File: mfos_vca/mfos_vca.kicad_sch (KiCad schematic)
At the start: 14 parts, among them J1 CV1, J2 CV1, Q1 2N3904, Q2 2N3906, SW1 SW_SPDT, U1 TL074

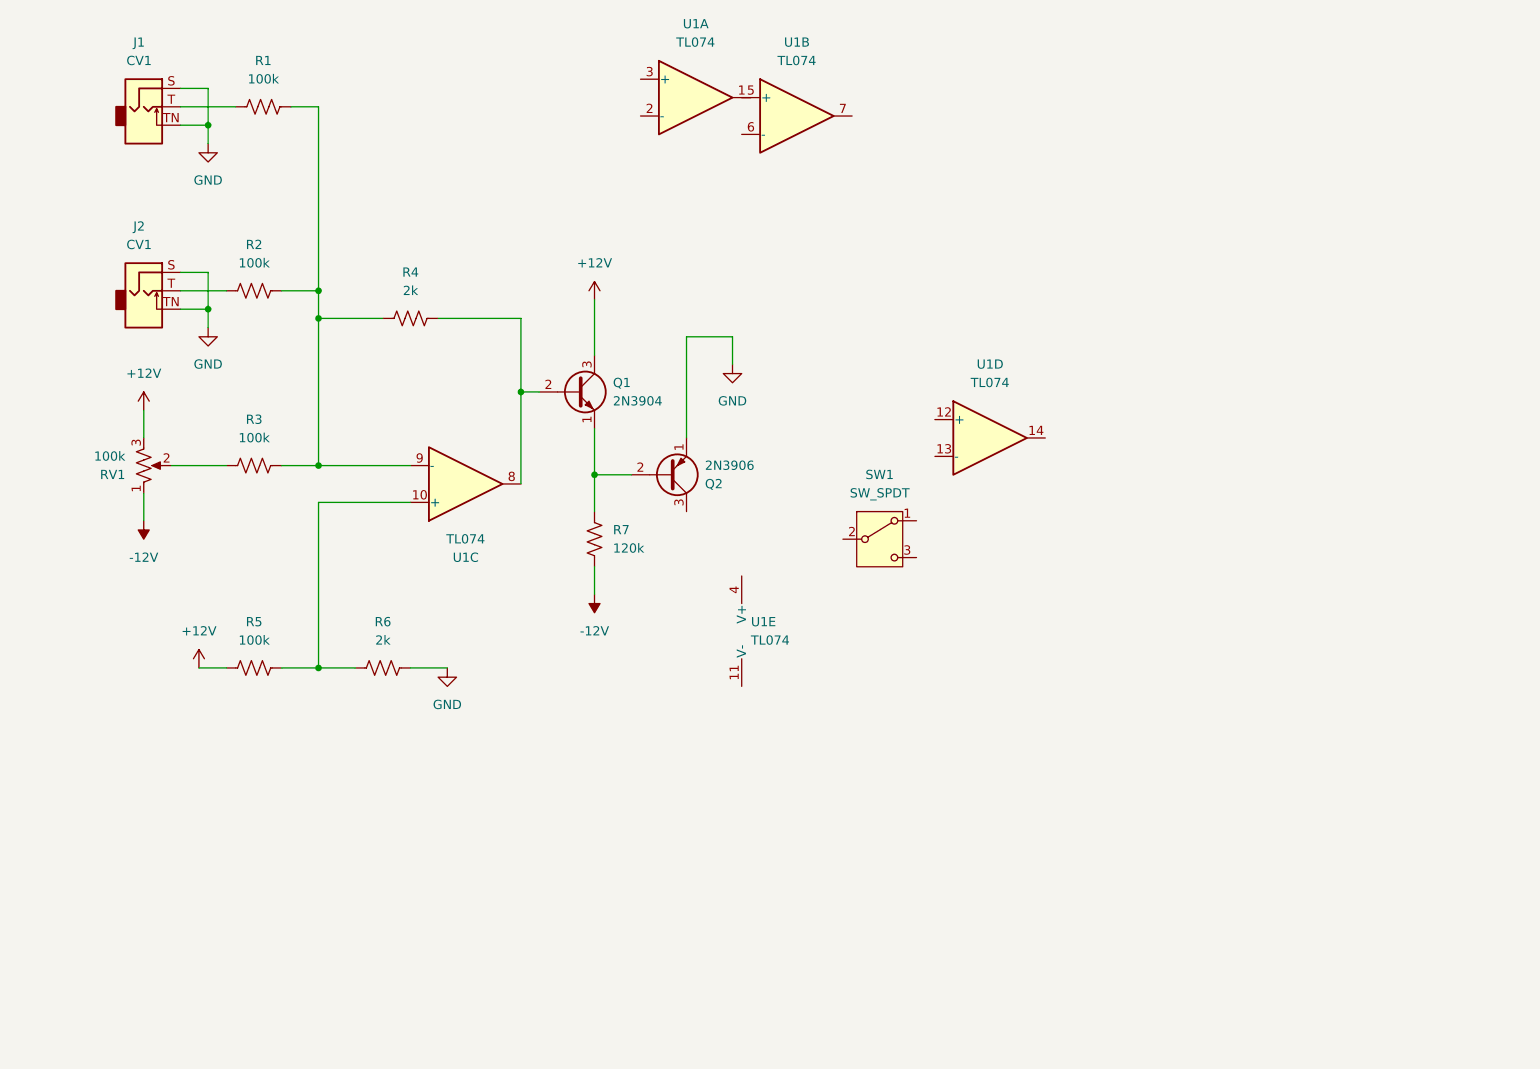
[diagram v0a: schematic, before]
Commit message: Mostly finish VCA-A schematic
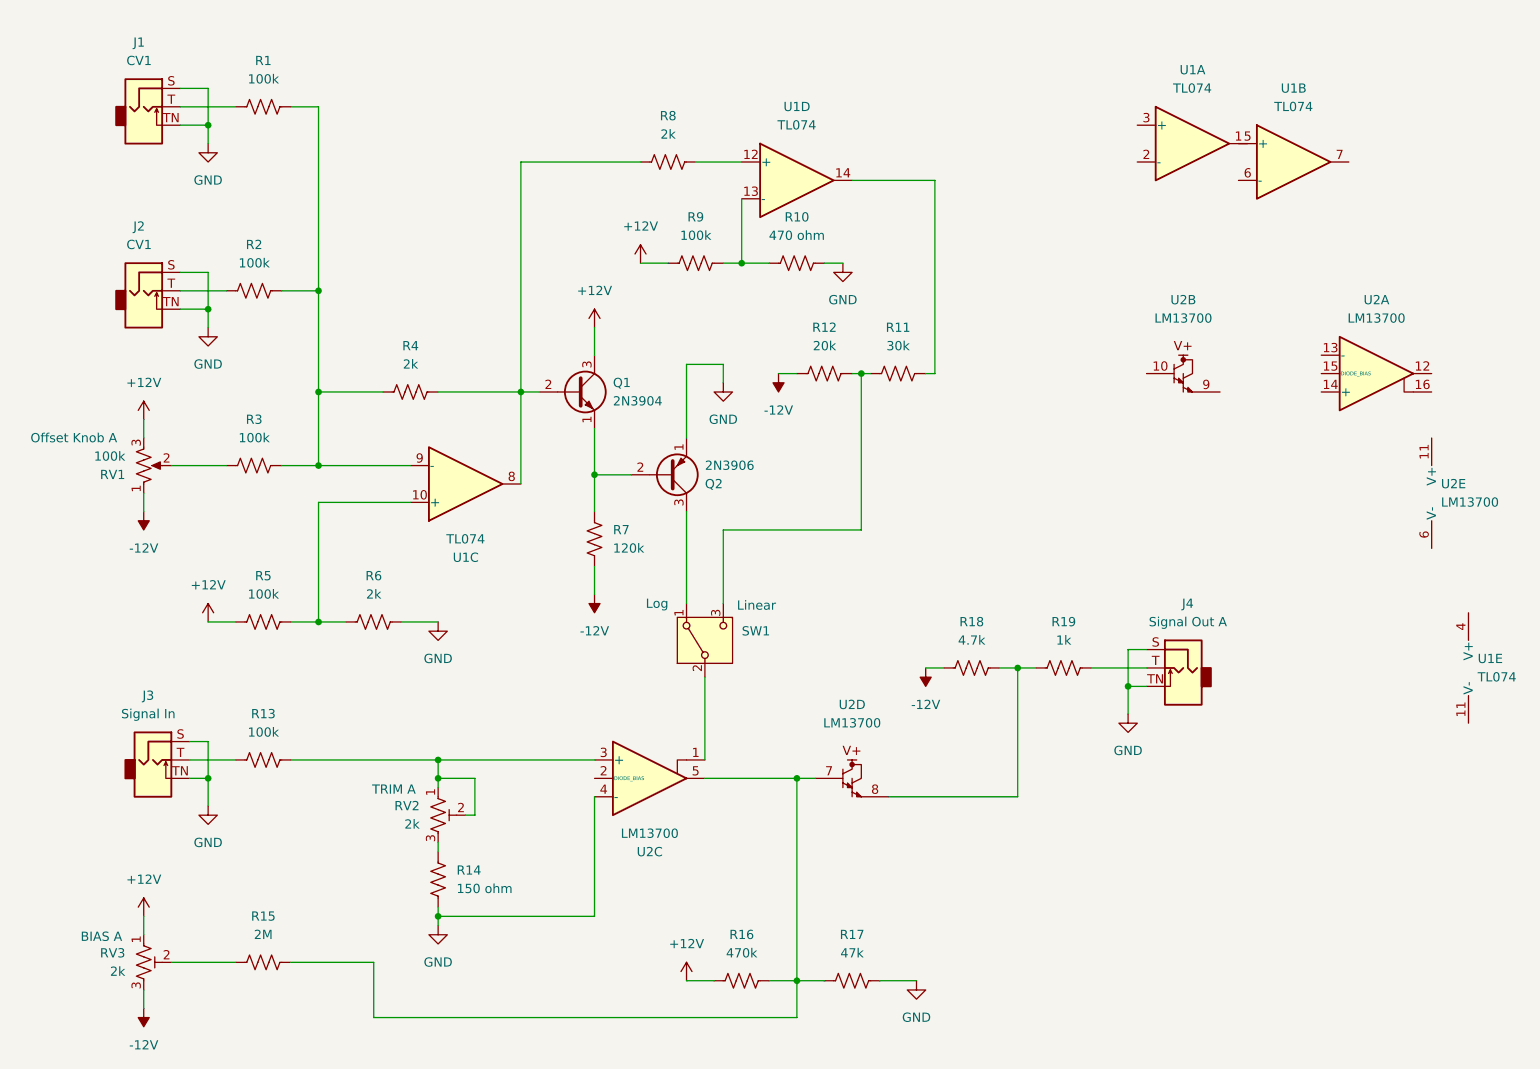
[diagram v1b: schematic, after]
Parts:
- added J3: Signal In, symbol Connector_Audio:AudioJack2_SwitchT
- added J4: Signal Out A, symbol Connector_Audio:AudioJack2_SwitchT
- added R10: 470 ohm, symbol Device:R_US
- added R11: 30k, symbol Device:R_US
- added R12: 20k, symbol Device:R_US
- added R13, R9: 100k, symbol Device:R_US
- added R14: 150 ohm, symbol Device:R_US
- added R15: 2M, symbol Device:R_US
- added R16: 470k, symbol Device:R_US
- added R17: 47k, symbol Device:R_US
- added R18: 4.7k, symbol Device:R_US
- added R19: 1k, symbol Device:R_US
- added R8: 2k, symbol Device:R_US
- added RV2, RV3: 2k, symbol Device:R_Potentiometer_Trim_US
- added U2: LM13700, symbol Amplifier_Operational:LM13700
- RV1: Label (none) -> Offset Knob A
- SW1: Label1 (none) -> Log; Label2 (none) -> Linear
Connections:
- net +12V: now also R16.1, R9.1, RV3.1
- net -12V: now also R12.1, R18.1, RV3.3
- net GND: now also J3.S, J3.TN, J4.S, J4.TN, R10.2, R14.2, R17.2, U2.4 (-)
- net at Q2.3 (C): now also SW1.1 (A)
- net at Q1.2 (B), R4.2, U1.8: now also R8.1
- net at SW1.2 (B): now also U2.1
- net at SW1.3 (C): now also R11.1, R12.2
- net at U1.12 (+): now also R8.2
- net at U1.13 (-): now also R10.1, R9.2
- net at U1.14: now also R11.2
- new net: J3.T, R13.1
- new net: R13.2, RV2.1, RV2.2, U2.3 (+)
- new net: R15.2, R16.2, R17.1, U2.5, U2.7
- new net: R18.2, R19.1, U2.8
- new net: R15.1, RV3.2
- new net: R14.1, RV2.3
- new net: J4.T, R19.2
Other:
- company: (none) -> Jesse Holzman
- title: (none) -> MFOS Dual VCA
- moved on the sheet: R4, R5, R6, SW1, U1A, U1B, U1D, U1E

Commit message: Add schematic for  second VCA
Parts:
- added D1, D2: 1N5819, symbol Device:D_Schottky
- added J5: CV1 B, symbol Connector_Audio:AudioJack2_SwitchT
- added J6: CV2 B, symbol Connector_Audio:AudioJack2_SwitchT
- added J7: Signal In B, symbol Connector_Audio:AudioJack2_SwitchT
- added J8: Signal Out A, symbol Connector_Audio:AudioJack2_SwitchT
- added J?: Conn_02x05_Odd_Even, symbol Connector_Generic:Conn_02x05_Odd_Even
- added Q3: 2N3904, Package_TO_SOT_THT:TO-92_Inline, symbol Transistor_BJT:2N3904
- added Q4: 2N3906, Package_TO_SOT_THT:TO-92_Inline, symbol Transistor_BJT:2N3906
- added R20, R21, R22, R23, R24, R31: 100k, symbol Device:R_US
- added R25: 2M, symbol Device:R_US
- added R26, R27, R30: 2k, symbol Device:R_US
- added R28: 150 ohm, symbol Device:R_US
- added R29: 120k, symbol Device:R_US
- added R32: 470k, symbol Device:R_US
- added R33: 470 ohm, symbol Device:R_US
- added R34: 20k, symbol Device:R_US
- added R35: 47k, symbol Device:R_US
- added R36: 30k, symbol Device:R_US
- added R37: 4.7k, symbol Device:R_US
- added R38: 1k, symbol Device:R_US
- added RV4: 100k, symbol Device:R_Potentiometer_US
- added RV5, RV6: 2k, symbol Device:R_Potentiometer_Trim_US
- added SW2: SW_SPDT, symbol Switch:SW_SPDT
- J1: value CV1 -> CV1 A
- J2: value CV1 -> CV2 A
- J3: value Signal In -> Signal In A
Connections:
- net +12V: now also Q3.3 (C), R23.1, R31.1, R32.1, RV4.3, RV5.1
- net -12V: now also R29.1, R34.1, R37.1, RV4.1, RV5.3
- net GND: now also U2.14 (+), J5.S, J5.TN, J6.S, J6.TN, J7.S, J7.TN, J8.S, J8.TN, J?.3 (Pin_3), J?.4 (Pin_4), J?.5 (Pin_5), J?.6 (Pin_6), J?.7 (Pin_7), J?.8 (Pin_8), Q4.1 (E), R26.2, R28.2, R33.2, R35.2
- net at U2.10: now also U2.16, R25.2, R32.2, R35.1
- net at U2.9: now also R37.2, R38.1
- net at U2.12: now also SW2.2 (B)
- net at U2.13 (-): now also R24.2, RV6.1, RV6.2
- net at U1.1: now also R36.2
- net at U1.2 (-): now also R31.2, R33.1
- net at U1.3 (+): now also R30.2
- net at U1.5 (+): now also R20.2, R21.2, R22.2, R27.1
- net at U1.6 (-): now also R23.2, R26.1
- net at U1.7: now also Q3.2 (B), R27.2, R30.1
- new net: Q4.3 (C), SW2.1 (A)
- new net: R34.2, R36.1, SW2.3 (C)
- new net: J7.T, R24.1
- new net: R21.1, RV4.2
- new net: Q3.1 (E), Q4.2 (B), R29.2
- new net: D2.1 (K), J?.1 (Pin_1), J?.2 (Pin_2)
- new net: R28.1, RV6.3
- new net: J8.T, R38.2
- new net: J6.T, R20.1
- new net: R25.1, RV5.2
- new net: D1.2 (A), J?.10 (Pin_10), J?.9 (Pin_9)
- new net: J5.T, R22.1
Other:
- moved on the sheet: R15, RV3, U1A, U1B, U1E, U2A, U2B, U2D, U2E

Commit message: Finish VCA schematic
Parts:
- added C1, C2: 47uF, symbol Device:C_Polarized_Small_US
- added C3, C4, C5, C6, C7, C8: 0.1uF, symbol Device:C_Small
- added R39, R40: 10 ohm, symbol Device:R_US
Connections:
- net +12V: now also U1.4 (V+), U2.11 (V+), C1.1, C3.1, C5.1, C7.1, R39.2
- net -12V: now also U1.11 (V-), U2.6 (V-), C2.2, C4.2, C6.2, C8.2, R40.2
- net GND: now also C1.2, C2.1, C3.2, C4.1, C5.2, C6.1, C7.2, C8.1
- net at D2.2 (A): now also R40.1
- net at D1.1 (K): now also R39.1
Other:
- moved on the sheet: D1, D2, J1, J2, J3, J4, J5, J6, J7, J8, J?, Q1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

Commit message: Assign footprints
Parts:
- C1, C2: footprint (none) -> Capacitor_THT:CP_Radial_D6.3mm_P2.50mm
- C3, C4, C5, C6, C7, C8: footprint (none) -> Capacitor_THT:C_Rect_L7.2mm_W2.5mm_P5.00mm
- D1, D2: footprint (none) -> Diode_THT:D_DO-41_SOD81_P7.62mm_Horizontal
- J1, J2, J3, J4, J5, J6, J7, J8, RV1, RV4: footprint (none) -> Connector_PinHeader_2.54mm:PinHeader_1x03_P2.54mm_Vertical
- J9: renamed from J?; footprint (none) -> Connector_IDC:IDC-Header_2x05_P2.54mm_Vertical
- R1, R10, R11, R12, R13, R14, R15, R16, R17, R18, R19, R2, R20, R21, R22, R23, R24, R25, R26, R27, R28, R29, R3, R30, R31, R32, R33, R34, R35, R36, R37, R38, R39, R4, R40, R5, R6, R7, R8, R9: footprint (none) -> Resistor_THT:R_Axial_DIN0207_L6.3mm_D2.5mm_P10.16mm_Horizontal
- RV2, RV6: footprint (none) -> Potentiometer_THT:Potentiometer_Bourns_3296W_Vertical
- RV3, RV5: value 2k -> 100k; footprint (none) -> Potentiometer_THT:Potentiometer_Piher_PT-6-V_Vertical
- U1: footprint (none) -> Package_DIP:DIP-14_W7.62mm_Socket
- U2: footprint (none) -> Package_DIP:DIP-16_W7.62mm_Socket

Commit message: Remove secondary CV input per VCA, some more panel progress
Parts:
- removed J1: CV1 A, Connector_PinHeader_2.54mm:PinHeader_1x03_P2.54mm_Vertical, symbol Connector_Audio:AudioJack2_SwitchT
- removed J5: CV1 B, Connector_PinHeader_2.54mm:PinHeader_1x03_P2.54mm_Vertical, symbol Connector_Audio:AudioJack2_SwitchT
- removed R1, R22: 100k, Resistor_THT:R_Axial_DIN0207_L6.3mm_D2.5mm_P10.16mm_Horizontal, symbol Device:R_US
- renumbered J2 to J1, J3 to J2, J4 to J3, J6 to J4, J7 to J5, J8 to J6, J9 to J7

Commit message: More progress, got rid of second cv input
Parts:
- J1: value CV2 A -> CV A; footprint Connector_PinHeader_2.54mm:PinHeader_1x03_P2.54mm_Vertical -> Library:PinHeader_1x03_P2.54mm_Vertical_AudioJack
- J2, J3, J5: footprint Connector_PinHeader_2.54mm:PinHeader_1x03_P2.54mm_Vertical -> Library:PinHeader_1x03_P2.54mm_Vertical_AudioJack
- J4: value CV2 B -> CV B; footprint Connector_PinHeader_2.54mm:PinHeader_1x03_P2.54mm_Vertical -> Library:PinHeader_1x03_P2.54mm_Vertical_AudioJack
- J6: value Signal Out A -> Signal Out B; footprint Connector_PinHeader_2.54mm:PinHeader_1x03_P2.54mm_Vertical -> Library:PinHeader_1x03_P2.54mm_Vertical_AudioJack
- SW1, SW2: footprint (none) -> Connector_PinHeader_2.54mm:PinHeader_1x03_P2.54mm_Vertical
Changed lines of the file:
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@@
 			)
 		)
-		(property "Footprint" ""
+		(property "Footprint" "Connector_PinHeader_2.54mm:PinHeader_1x03_P2.54mm_Vertical"
 			(at 317.5 107.95 0)
 			(effects
@@
 			)
 		)
-		(property "Value" "CV2 A"
+		(property "Value" "CV A"
 			(at 41.275 54.61 0)
 			(effects
@@
 			)
 		)
-		(property "Footprint" "Connector_PinHeader_2.54mm:PinHeader_1x03_P2.54mm_Vertical"
+		(property "Footprint" "Library:PinHeader_1x03_P2.54mm_Vertical_AudioJack"
 			(at 41.91 60.96 0)
 			(effects
@@
 			)
 		)
-		(property "Footprint" "Connector_PinHeader_2.54mm:PinHeader_1x03_P2.54mm_Vertical"
+		(property "Footprint" "Library:PinHeader_1x03_P2.54mm_Vertical_AudioJack"
 			(at 241.3 124.46 0)
 			(effects
@@
 			)
 		)
-		(property "Footprint" ""
+		(property "Footprint" "Connector_PinHeader_2.54mm:PinHeader_1x03_P2.54mm_Vertical"
 			(at 119.38 109.22 0)
 			(effects
@@
 			)
 		)
-		(property "Value" "Signal Out A"
+		(property "Value" "Signal Out B"
 			(at 384.175 105.41 0)
 			(effects
@@
 			)
 		)
-		(property "Footprint" "Connector_PinHeader_2.54mm:PinHeader_1x03_P2.54mm_Vertical"
+		(property "Footprint" "Library:PinHeader_1x03_P2.54mm_Vertical_AudioJack"
 			(at 383.54 111.76 0)
 			(effects
@@
 			)
 		)
-		(property "Footprint" "Connector_PinHeader_2.54mm:PinHeader_1x03_P2.54mm_Vertical"
+		(property "Footprint" "Library:PinHeader_1x03_P2.54mm_Vertical_AudioJack"
 			(at 185.42 113.03 0)
 			(effects
@@
 			)
 		)
-		(property "Footprint" "Connector_PinHeader_2.54mm:PinHeader_1x03_P2.54mm_Vertical"
+		(property "Footprint" "Library:PinHeader_1x03_P2.54mm_Vertical_AudioJack"
 			(at 43.18 125.73 0)
 			(effects
@@
 			)
 		)
-		(property "Value" "CV2 B"
+		(property "Value" "CV B"
 			(at 239.395 53.34 0)
 			(effects
@@
 			)
 		)
-		(property "Footprint" "Connector_PinHeader_2.54mm:PinHeader_1x03_P2.54mm_Vertical"
+		(property "Footprint" "Library:PinHeader_1x03_P2.54mm_Vertical_AudioJack"
 			(at 240.03 59.69 0)
 			(effects

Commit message: Almost done all of the tracks in vca pcb, fix the custom library footprint
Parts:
- J1, J2, J3, J4, J5, J6: footprint Library:PinHeader_1x03_P2.54mm_Vertical_AudioJack -> CustomStuff:PinHeader_1x03_P2.54mm_Vertical_AudioJack
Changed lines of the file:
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@@
 			)
 		)
-		(property "Footprint" "Library:PinHeader_1x03_P2.54mm_Vertical_AudioJack"
+		(property "Footprint" "CustomStuff:PinHeader_1x03_P2.54mm_Vertical_AudioJack"
 			(at 41.91 60.96 0)
 			(effects
@@
 			)
 		)
-		(property "Footprint" "Library:PinHeader_1x03_P2.54mm_Vertical_AudioJack"
+		(property "Footprint" "CustomStuff:PinHeader_1x03_P2.54mm_Vertical_AudioJack"
 			(at 241.3 124.46 0)
 			(effects
@@
 			)
 		)
-		(property "Footprint" "Library:PinHeader_1x03_P2.54mm_Vertical_AudioJack"
+		(property "Footprint" "CustomStuff:PinHeader_1x03_P2.54mm_Vertical_AudioJack"
 			(at 383.54 111.76 0)
 			(effects
@@
 			)
 		)
-		(property "Footprint" "Library:PinHeader_1x03_P2.54mm_Vertical_AudioJack"
+		(property "Footprint" "CustomStuff:PinHeader_1x03_P2.54mm_Vertical_AudioJack"
 			(at 185.42 113.03 0)
 			(effects
@@
 			)
 		)
-		(property "Footprint" "Library:PinHeader_1x03_P2.54mm_Vertical_AudioJack"
+		(property "Footprint" "CustomStuff:PinHeader_1x03_P2.54mm_Vertical_AudioJack"
 			(at 43.18 125.73 0)
 			(effects
@@
 			)
 		)
-		(property "Footprint" "Library:PinHeader_1x03_P2.54mm_Vertical_AudioJack"
+		(property "Footprint" "CustomStuff:PinHeader_1x03_P2.54mm_Vertical_AudioJack"
 			(at 240.03 59.69 0)
 			(effects

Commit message: fix a couple stupid mistakes in schematic
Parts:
- added R13, R32: 100k, Resistor_THT:R_Axial_DIN0207_L6.3mm_D2.5mm_P10.16mm_Horizontal, symbol Device:R_US
- renumbered R2 to R1, R8 to R10, R9 to R11, R16 to R12, R10 to R14, R12 to R15, R17 to R16, R11 to R17, R3 to R2, R23 to R22, R24 to R23, R25 to R24, R26 to R25, R27 to R26, R28 to R27, R29 to R28, R30 to R29, R5 to R3, R31 to R30, R32 to R31, R13 to R4, R15 to R5, R4 to R7, R14 to R8, R7 to R9, RV3 to RV2, RV2 to RV3
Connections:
- net GND: now also U2.13 (-); no longer U2.14 (+)
- net at SW2.2 (B): now also U2.16; no longer U2.12
- net at R29.2: now also U1.2 (-), R32.1; no longer U1.3 (+)
- net at R24.2, R31.2, R35.1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: now also U2.12; no longer U2.16
- net at R23.2, RV6.1, RV6.2: now also U2.14 (+); no longer U2.13 (-)
- net at R20.2, R21.2, R26.1: now also U1.6 (-); no longer U1.5 (+)
- net at R10.2: now also U1.13 (-), R13.1; no longer U1.12 (+)
- net at R36.2, U1.1: now also R32.2
- net at R30.2, R33.1: now also U1.3 (+); no longer U1.2 (-)
- net at R22.2, R25.1: now also U1.5 (+); no longer U1.6 (-)
- net at R11.2, R14.1: now also U1.12 (+); no longer U1.13 (-)
- net at R17.2, U1.14: now also R13.2
